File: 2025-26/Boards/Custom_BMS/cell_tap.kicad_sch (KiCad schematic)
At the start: 50 parts

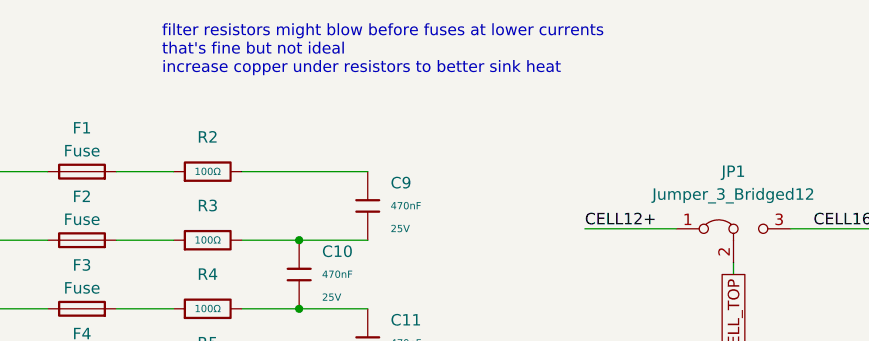
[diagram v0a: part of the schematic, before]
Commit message: designed power circuitry
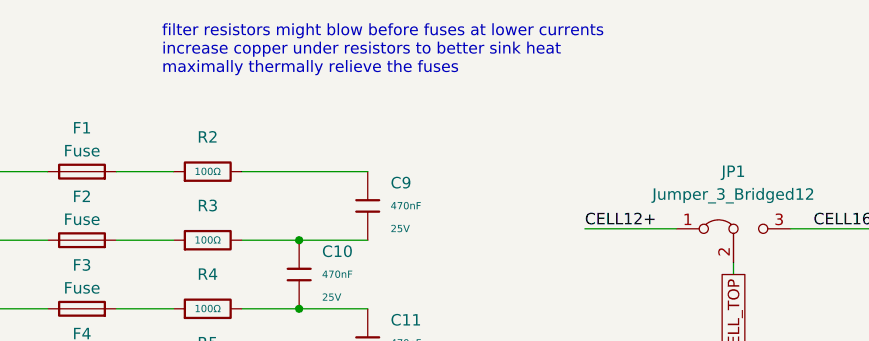
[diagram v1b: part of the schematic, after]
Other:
- note added: "filter resistors might blow before fuses at lower currents increase copper under resistors to better sink heat maximally thermally relieve the fuses"
- note removed: "filter resistors might blow before fuses at lower currents that's fine but not ideal increase copper under resistors to better sink heat"
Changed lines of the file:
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@@
 		)
 	)
-	(text "filter resistors might blow before fuses at lower currents\nthat's fine but not ideal\nincrease copper under resistors to better sink heat"
+	(text "filter resistors might blow before fuses at lower currents\nincrease copper under resistors to better sink heat\nmaximally thermally relieve the fuses"
 		(exclude_from_sim no)
 		(at 135.89 38.608 0)

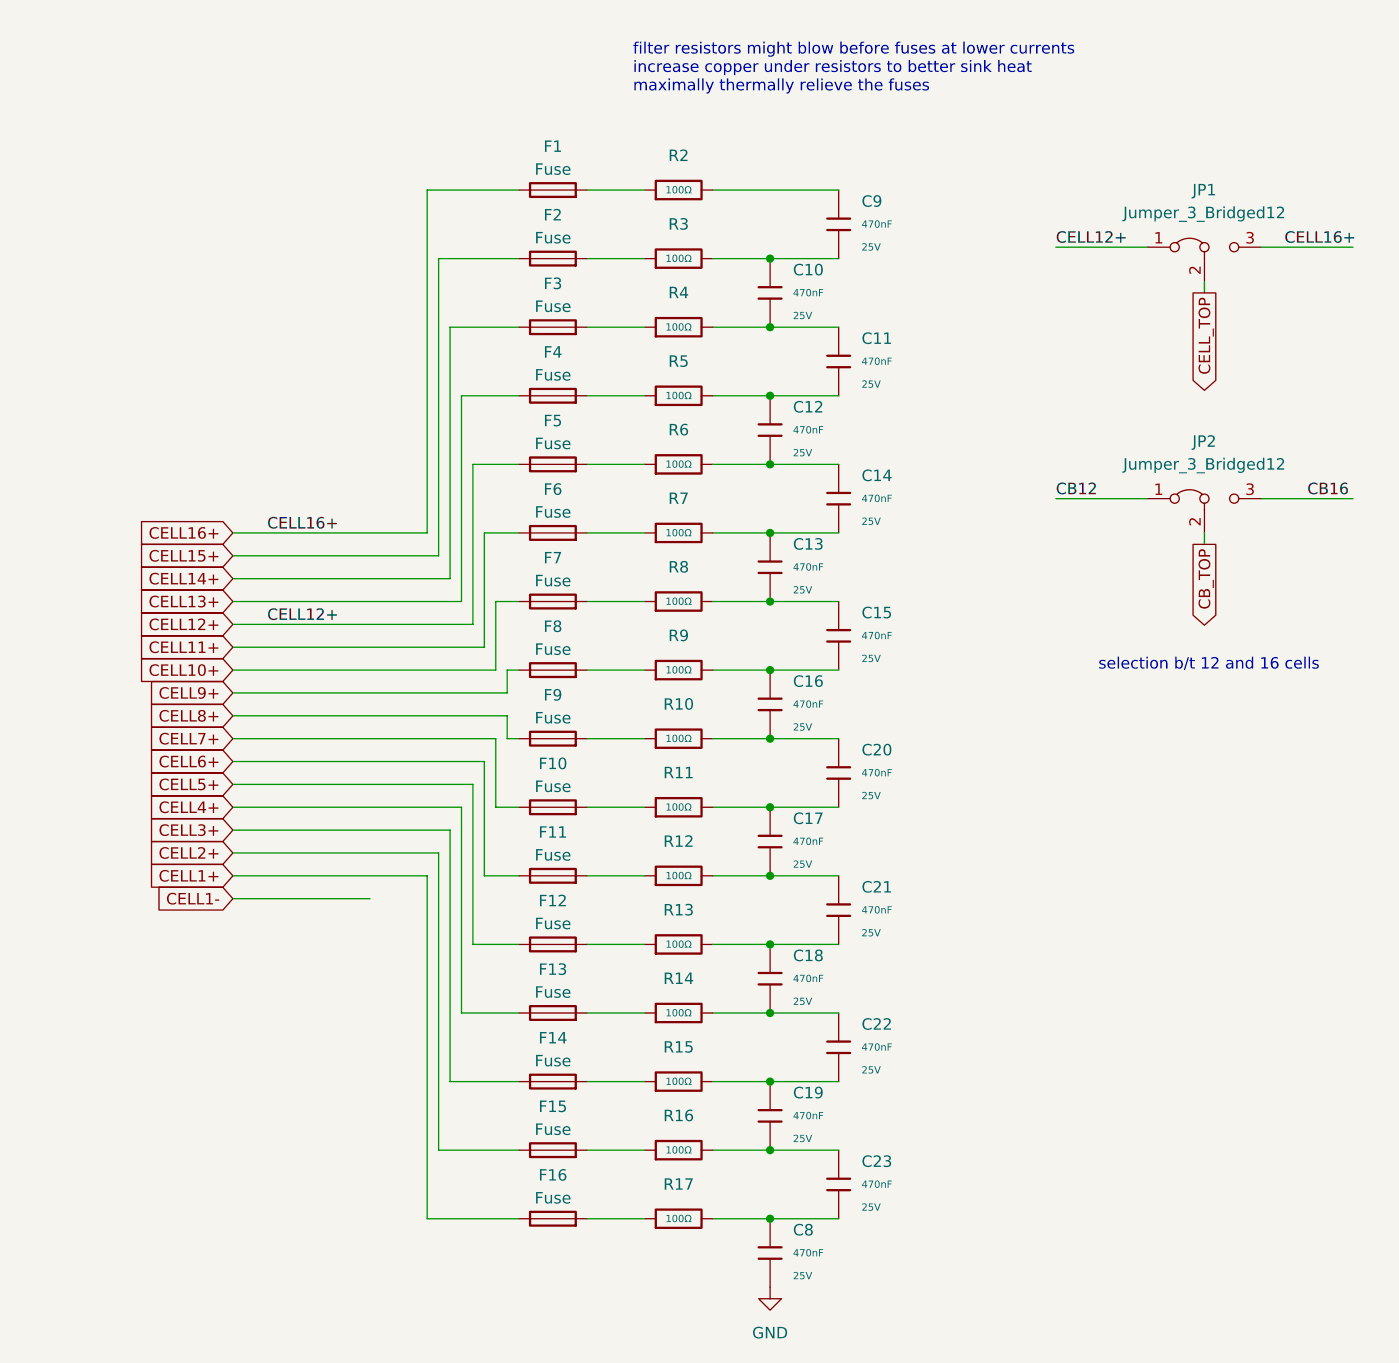
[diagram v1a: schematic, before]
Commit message: fixed some net names
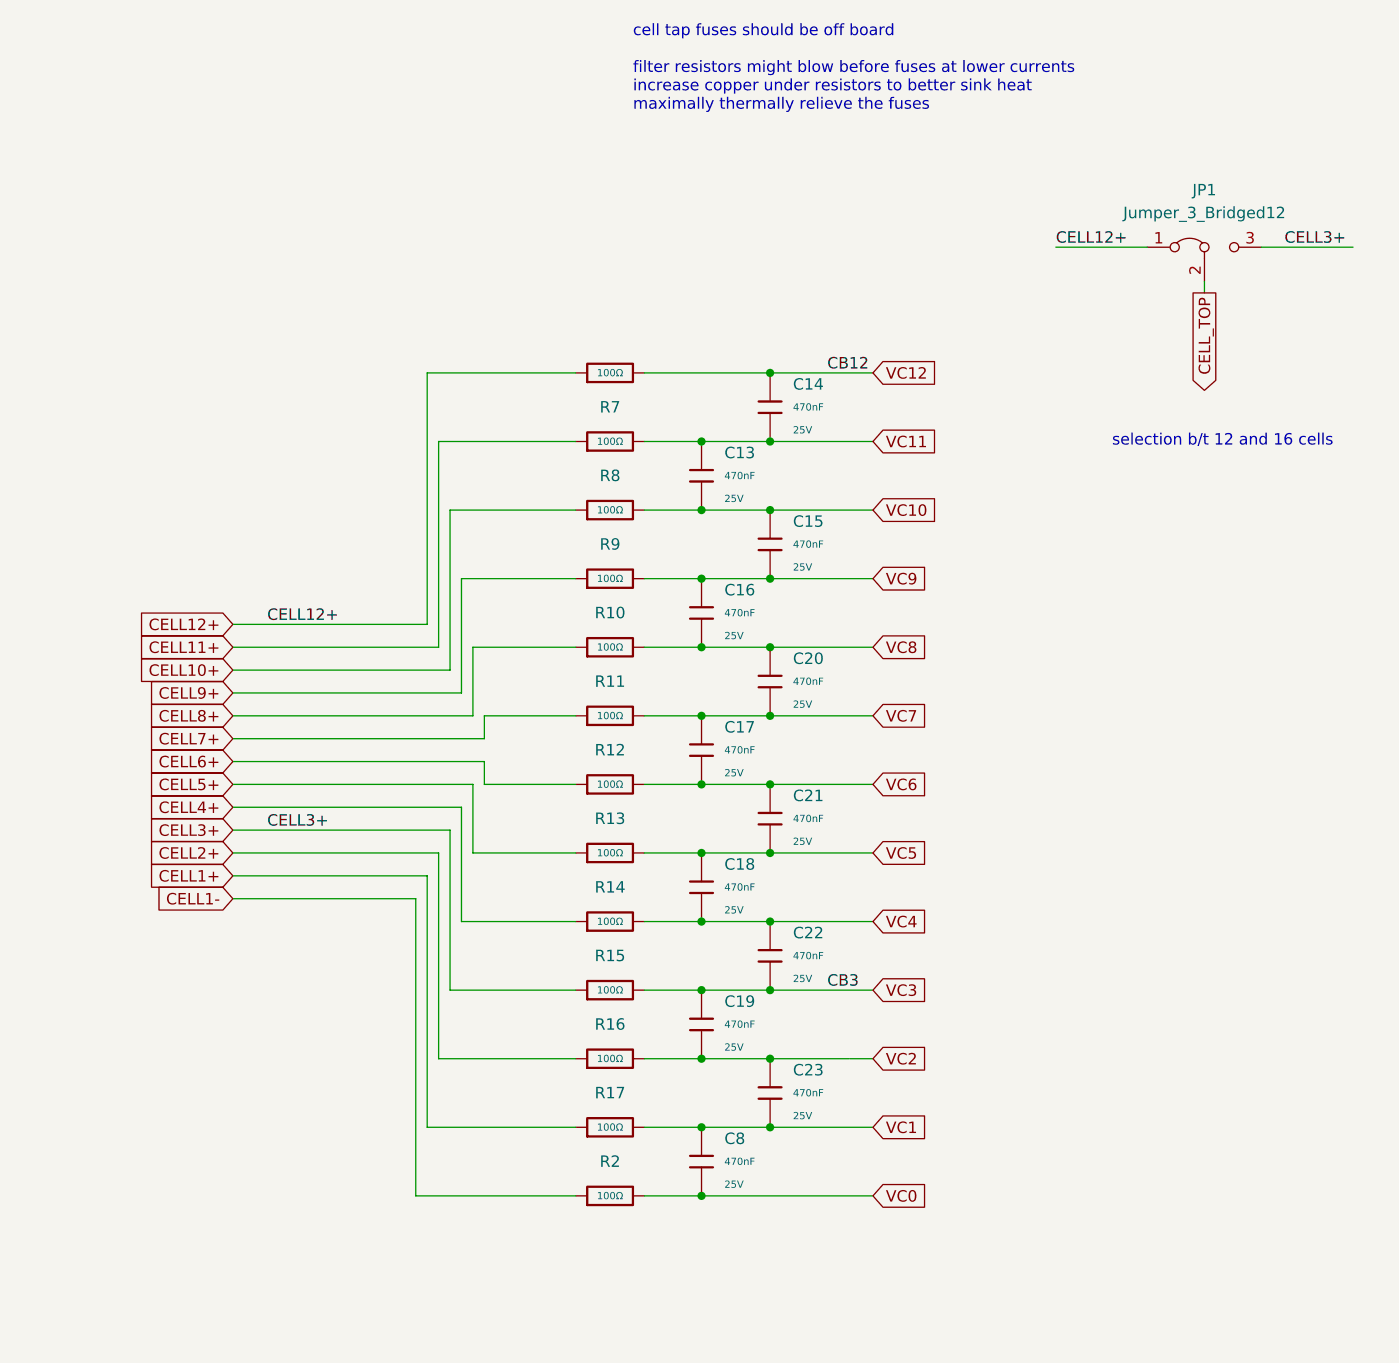
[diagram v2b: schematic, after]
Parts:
- removed C10, C11, C12, C9: 470nF, PCM_JLCPCB:C_0603, symbol PCM_JLCPCB-Capacitors:0603,470nF
- removed F1, F10, F11, F12, F13, F14, F15, F16, F2, F3, F4, F5, F6, F7, F8, F9: Fuse, symbol Device:Fuse
- removed JP2: Jumper_3_Bridged12, symbol Jumper:Jumper_3_Bridged12
- removed R3, R4, R5: 100Ω, PCM_JLCPCB:R_0603, symbol PCM_JLCPCB-Resistors:0603,100Ω
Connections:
- net CELL16+ is gone; now on net CELL3+: JP1.3 (B)
- net GND is gone; now on net VC0: C8.2
- net CELL1+: now also R17.1
- net CELL1-: now also R2.1
- net CELL10+: now also R8.1
- net CELL11+: now also R7.1
- net CELL12+: now also R6.1
- net CELL2+: now also R16.1
- net CELL3+: now also R15.1
- net CELL4+: now also R14.1
- net CELL5+: now also R13.1
- net CELL6+: now also R12.1
- net CELL7+: now also R11.1
- net CELL8+: now also R10.1
- net CELL9+: now also R9.1
- net VC9: now reaches C15.2, C16.1, R9.2
- net VC8: now reaches C16.2, C20.1, R10.2
- net VC10: now reaches C13.2, C15.1, R8.2
- net VC12: now reaches C14.1, R6.2
- net VC11: now reaches C13.1, C14.2, R7.2
- net VC3: now reaches C19.1, C22.2, R15.2
- net VC0: now reaches R2.2
- net VC1: now reaches C23.2, C8.1, R17.2
- net VC6: now reaches C17.2, C21.1, R12.2
- net VC5: now reaches C18.1, C21.2, R13.2
- net VC4: now reaches C18.2, C22.1, R14.2
- net VC7: now reaches C17.1, C20.2, R11.2
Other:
- note added: "cell tap fuses should be off board filter resistors might blow before fuses at lower currents increase copper under resistors to better sink heat maximally thermally relieve the fuses"
- note removed: "filter resistors might blow before fuses at lower currents increase copper under resistors to better sink heat maximally thermally relieve the fuses"
- moved on the sheet: C13, C14, C15, C16, C17, C18, C19, C20, C21, C22, C23, C8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

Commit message: started layout
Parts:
- JP1: footprint (none) -> Connector_PinHeader_2.00mm:PinHeader_1x03_P2.00mm_Vertical
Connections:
- net VC2: now also C19.2, C23.1, R16.2
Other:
- moved on the sheet: C13, C14, C15, C16, C17, C18, C19, C20, C21, C22, C23, C8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

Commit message: more layout progress
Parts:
- added C72: 470nF, PCM_JLCPCB:C_0603, symbol PCM_JLCPCB-Capacitors:0603,470nF
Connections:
- net VC0: now also C72.1
- net CELL1- renamed GND
- net GND: now also C72.2

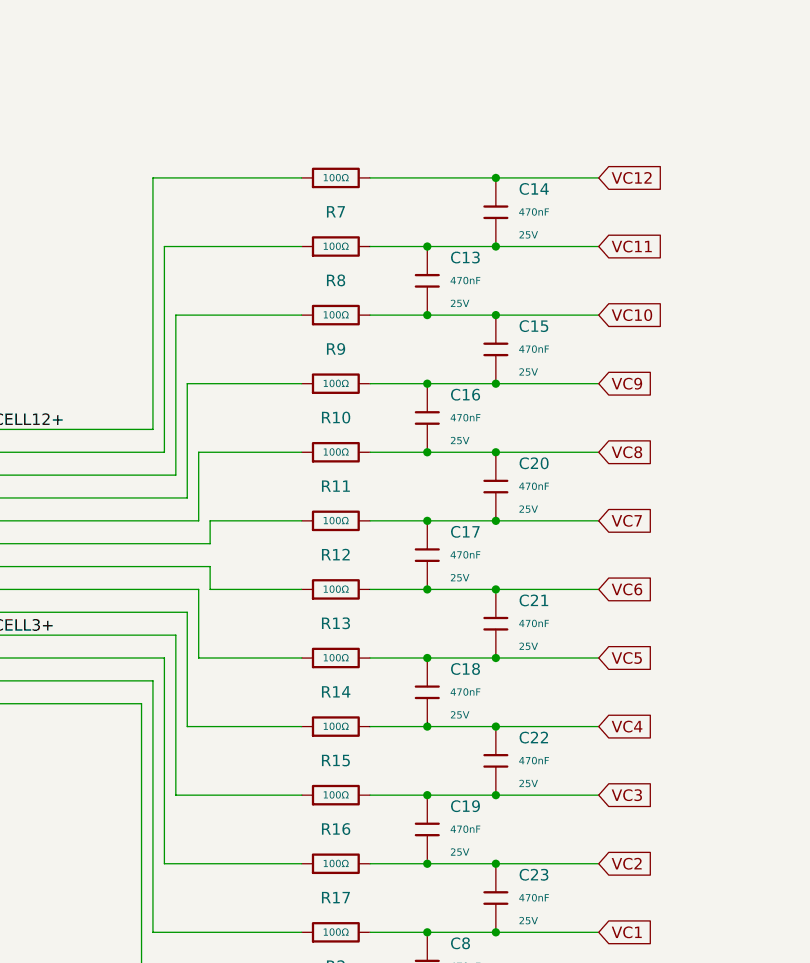
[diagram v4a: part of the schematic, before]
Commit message: fixed some layout and schematic issues
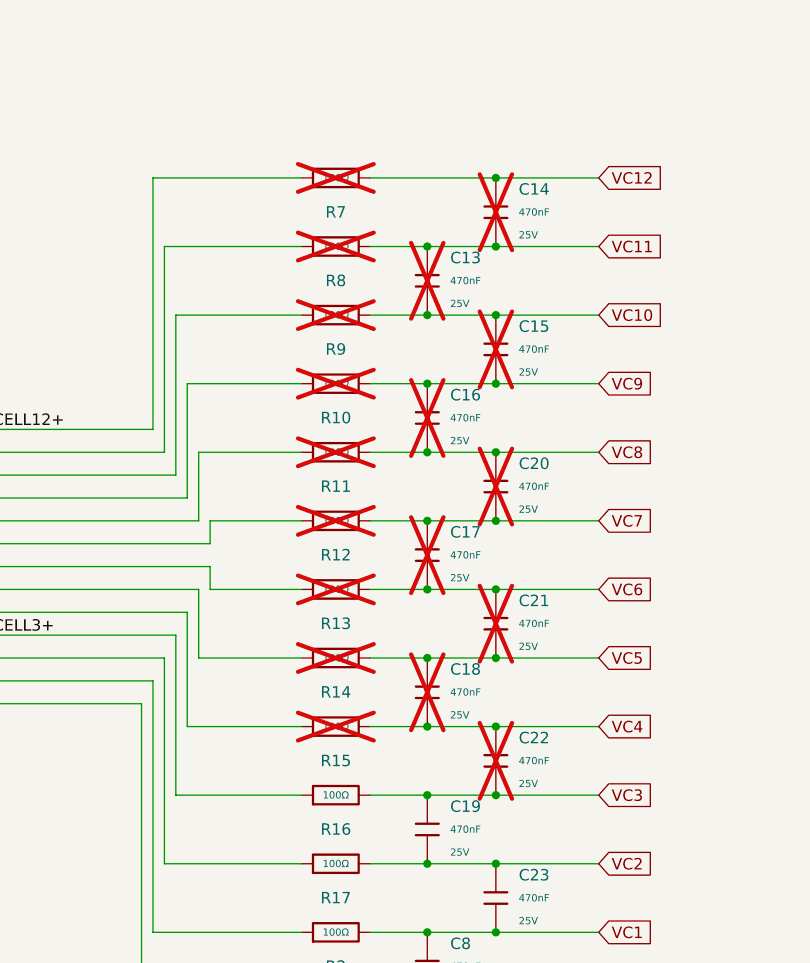
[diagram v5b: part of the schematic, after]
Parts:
- C13, C14, C15, C16, C17, C18, C20, C21, C22, R10, R11, R12, R13, R14, R6, R7, R8, R9: now not fitted; now left out of the parts list
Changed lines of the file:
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@@
 		(unit 1)
 		(exclude_from_sim no)
-		(in_bom yes)
+		(in_bom no)
 		(on_board yes)
-		(dnp no)
+		(dnp yes)
 		(fields_autoplaced yes)
 		(property "Reference" "C16"
@@
 		(unit 1)
 		(exclude_from_sim no)
-		(in_bom yes)
+		(in_bom no)
 		(on_board yes)
-		(dnp no)
+		(dnp yes)
 		(fields_autoplaced yes)
 		(property "Reference" "R8"
@@
 		(unit 1)
 		(exclude_from_sim no)
-		(in_bom yes)
+		(in_bom no)
 		(on_board yes)
-		(dnp no)
+		(dnp yes)
 		(fields_autoplaced yes)
 		(property "Reference" "R9"
@@
 		(unit 1)
 		(exclude_from_sim no)
-		(in_bom yes)
+		(in_bom no)
 		(on_board yes)
-		(dnp no)
+		(dnp yes)
 		(fields_autoplaced yes)
 		(property "Reference" "C14"
@@
 		(unit 1)
 		(exclude_from_sim no)
-		(in_bom yes)
+		(in_bom no)
 		(on_board yes)
-		(dnp no)
+		(dnp yes)
 		(fields_autoplaced yes)
 		(property "Reference" "R10"
@@
 		(unit 1)
 		(exclude_from_sim no)
-		(in_bom yes)
+		(in_bom no)
 		(on_board yes)
-		(dnp no)
+		(dnp yes)
 		(fields_autoplaced yes)
 		(property "Reference" "R7"
@@
 		(unit 1)
 		(exclude_from_sim no)
-		(in_bom yes)
+		(in_bom no)
 		(on_board yes)
-		(dnp no)
+		(dnp yes)
 		(fields_autoplaced yes)
 		(property "Reference" "C21"
@@
 		(unit 1)
 		(exclude_from_sim no)
-		(in_bom yes)
+		(in_bom no)
 		(on_board yes)
-		(dnp no)
+		(dnp yes)
 		(fields_autoplaced yes)
 		(property "Reference" "R6"
@@
 		(unit 1)
 		(exclude_from_sim no)
-		(in_bom yes)
+		(in_bom no)
 		(on_board yes)
-		(dnp no)
+		(dnp yes)
 		(fields_autoplaced yes)
 		(property "Reference" "C22"
@@
 		(unit 1)
 		(exclude_from_sim no)
-		(in_bom yes)
+		(in_bom no)
 		(on_board yes)
-		(dnp no)
+		(dnp yes)
 		(fields_autoplaced yes)
 		(property "Reference" "R12"
@@
 		(unit 1)
 		(exclude_from_sim no)
-		(in_bom yes)
+		(in_bom no)
 		(on_board yes)
-		(dnp no)
+		(dnp yes)
 		(fields_autoplaced yes)
 		(property "Reference" "C20"
@@
 		(unit 1)
 		(exclude_from_sim no)
-		(in_bom yes)
+		(in_bom no)
 		(on_board yes)
-		(dnp no)
+		(dnp yes)
 		(fields_autoplaced yes)
 		(property "Reference" "C18"
@@
 		(unit 1)
 		(exclude_from_sim no)
-		(in_bom yes)
+		(in_bom no)
 		(on_board yes)
-		(dnp no)
+		(dnp yes)
 		(fields_autoplaced yes)
 		(property "Reference" "R13"
@@
 		(unit 1)
 		(exclude_from_sim no)
-		(in_bom yes)
+		(in_bom no)
 		(on_board yes)
-		(dnp no)
+		(dnp yes)
 		(fields_autoplaced yes)
 		(property "Reference" "R14"
@@
 		(unit 1)
 		(exclude_from_sim no)
-		(in_bom yes)
+		(in_bom no)
 		(on_board yes)
-		(dnp no)
+		(dnp yes)
 		(fields_autoplaced yes)
 		(property "Reference" "C15"
@@
 		(unit 1)
 		(exclude_from_sim no)
-		(in_bom yes)
+		(in_bom no)
 		(on_board yes)
-		(dnp no)
+		(dnp yes)
 		(fields_autoplaced yes)
 		(property "Reference" "R11"
@@
 		(unit 1)
 		(exclude_from_sim no)
-		(in_bom yes)
+		(in_bom no)
 		(on_board yes)
-		(dnp no)
+		(dnp yes)
 		(fields_autoplaced yes)
 		(property "Reference" "C17"
@@
 		(unit 1)
 		(exclude_from_sim no)
-		(in_bom yes)
+		(in_bom no)
 		(on_board yes)
-		(dnp no)
+		(dnp yes)
 		(fields_autoplaced yes)
 		(property "Reference" "C13"

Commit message: fixed review items
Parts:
- C22, R14: now fitted; now in the parts list
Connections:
- net CELL3+: no longer JP1.3 (B)
- net CELL4+: now also JP1.3 (B)
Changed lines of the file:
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@@
 		)
 	)
-	(label "CELL3+"
+	(label "CELL4+"
 		(at 208.28 58.42 0)
 		(effects
@@
 		(unit 1)
 		(exclude_from_sim no)
-		(in_bom no)
+		(in_bom yes)
 		(on_board yes)
-		(dnp yes)
+		(dnp no)
 		(fields_autoplaced yes)
 		(property "Reference" "C22"
@@
 		(unit 1)
 		(exclude_from_sim no)
-		(in_bom no)
+		(in_bom yes)
 		(on_board yes)
-		(dnp yes)
+		(dnp no)
 		(fields_autoplaced yes)
 		(property "Reference" "R14"

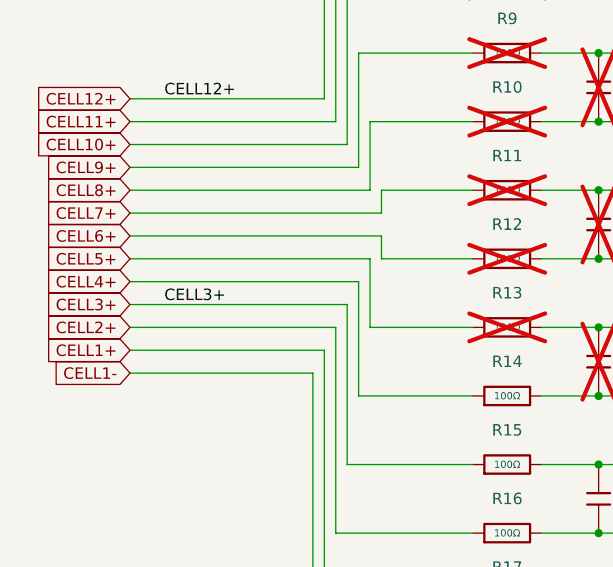
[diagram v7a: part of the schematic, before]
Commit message: fixed some connectors
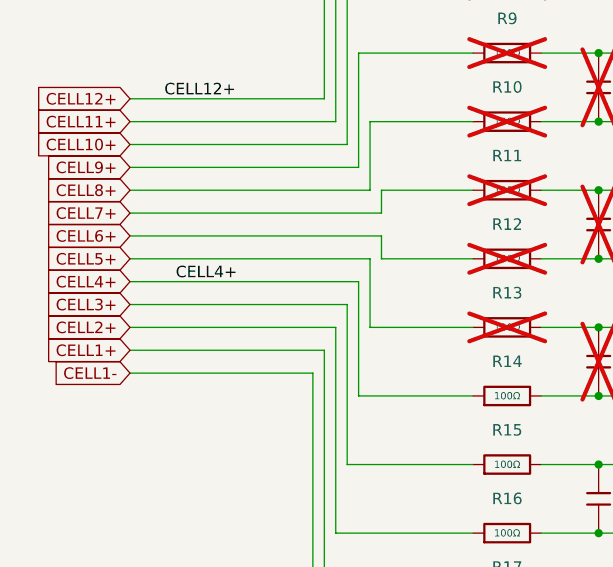
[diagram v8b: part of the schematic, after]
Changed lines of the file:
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@@
 		)
 	)
-	(label "CELL3+"
-		(at 83.82 116.84 0)
+	(label "CELL4+"
+		(at 85.09 114.3 0)
 		(effects
 			(font
